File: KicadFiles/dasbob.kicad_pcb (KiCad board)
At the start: 2 copper layers, 243.5 x 104.8 mm, 64 parts, among them J1 TRRS LEFT, J2 TRRS LEFT, SW1 SW_Push, SW10 SW_Push, SW11 SW_Push, SW12 SW_Push, SW13 SW_Push, SW14 SW_Push, SW15 SW_Push, SW16 SW_Push, SW17 SW_Push, SW18 SW_Push, SW19 SW_Push, SW2 SW_Push, SW20 SW_Push, SW21 SW_Push, SW22 SW_Push, SW23 SW_Push, SW24 SW_Push, SW25 SW_Push, SW26 SW_Push, SW27 SW_Push, SW28 SW_Push, SW29 SW_Push, SW3 SW_Push, SW30 SW_Push, SW31 SW_Push, SW32 SW_Push, SW33 SW_Push, SW34 SW_Push, SW35 SW_Push, SW36 SW_Push, SW4 SW_Push, SW5 SW_Push, SW6 SW_Push, SW7 SW_Push, SW8 SW_Push, SW9 SW_Push, U1 Elite-C RIGHT, U2 Elite-C LEFT, U3 OLED1, U4 OLED2

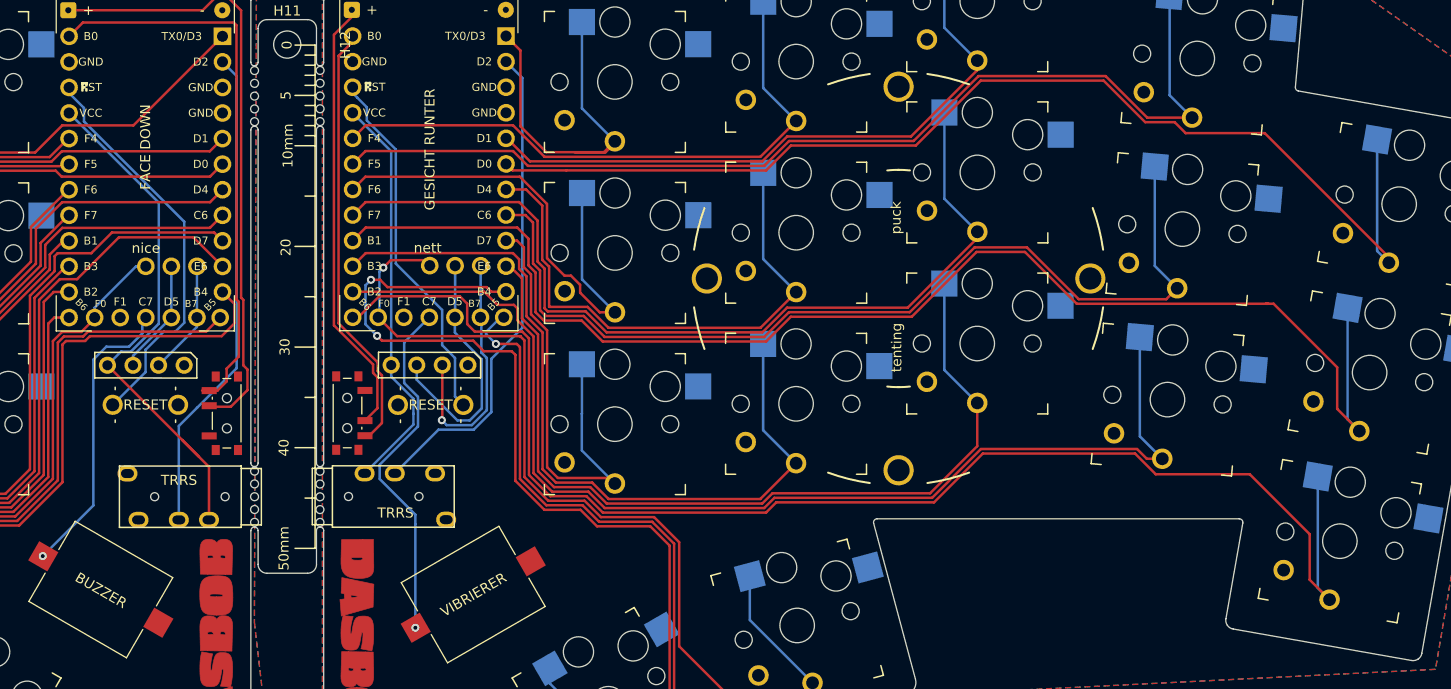
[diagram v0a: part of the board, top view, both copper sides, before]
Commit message: routed the oled to the wrong pins because im a ducking idiot now i fixed it
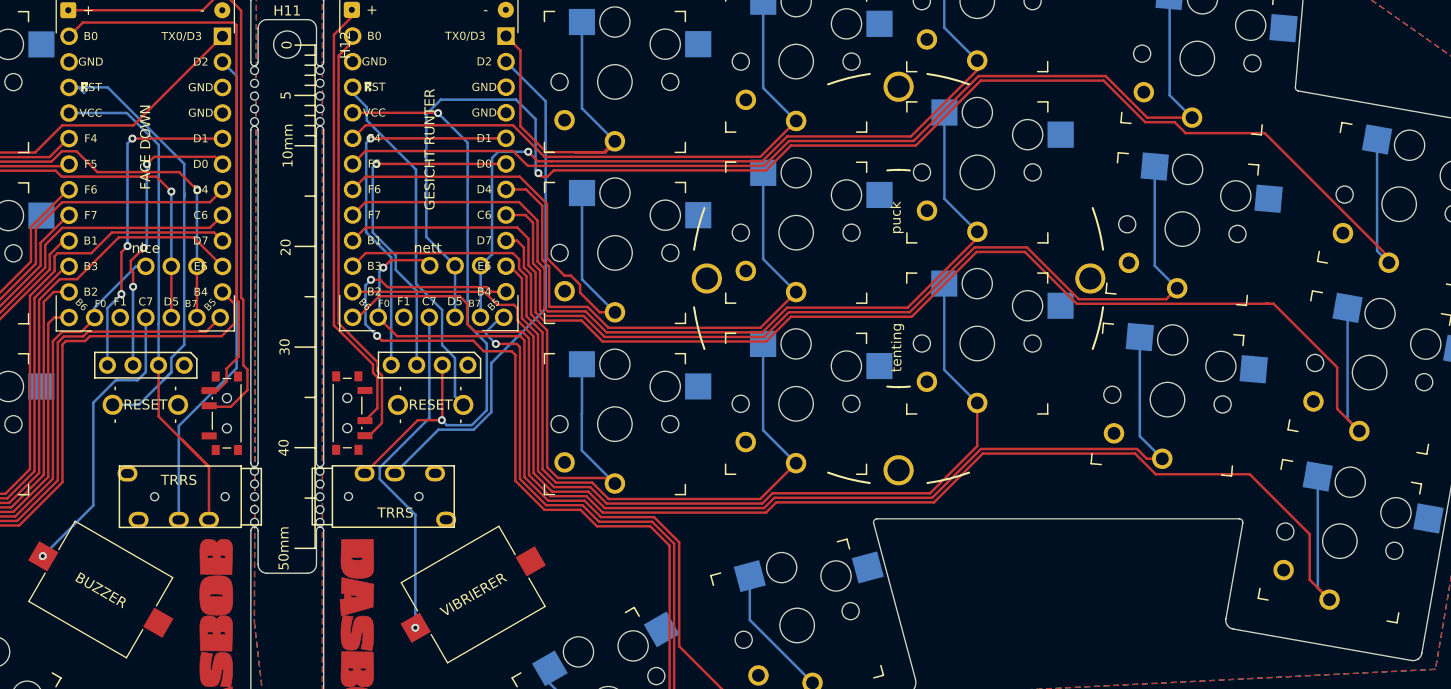
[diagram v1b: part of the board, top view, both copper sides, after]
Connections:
- H5 pad 1: P1 -> 3
- H6 pad 1: P2 -> 1
- H7 pad 1: 1P -> 3a
- H8 pad 1: 2P -> 1a
- U1 pad 25: P1 -> 3
- U1 pad 26: P2 -> 1
- U1 pad 5: 3 -> P1
- U1 pad 6: 1 -> P2
- U2 pad 25: 1P -> 3a
- U2 pad 26: 2P -> 1a
- U2 pad 5: 3a -> 1P
- U2 pad 6: 1a -> 2P
- U3 pad 2: P1 -> VCC
- U3 pad 4: VCC -> P1
- U4 pad 2: 1P -> CVV
- U4 pad 4: CVV -> 1P
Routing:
- net 1a: track 111.7 -> 147.7 mm, vias 0 -> 1
- net P1: track 11.4 -> 32.6 mm, vias 0 -> 3
- net CVV: track 40.3 -> 60.8 mm, vias 0 -> 2
- net 3a: track 65.7 -> 83.2 mm, vias 0 -> 1
- net P2: track 11.4 -> 28.9 mm, vias 0 -> 3
- net 1P: track 25.4 -> 37.3 mm
- net 3: track 80.5 -> 91.7 mm, vias 0 -> 1
- net 2P: track 25.4 -> 35.1 mm, vias 0 -> 1
- net 1: track 128.3 -> 135.9 mm, vias 0 -> 1
- net RST: track 39.2 -> 46.1 mm
- net VCC: track 53.3 -> 55.7 mm
- net 1R: track 48.9 -> 50.8 mm
- net DNUOS: track 35.5 -> 34.4 mm

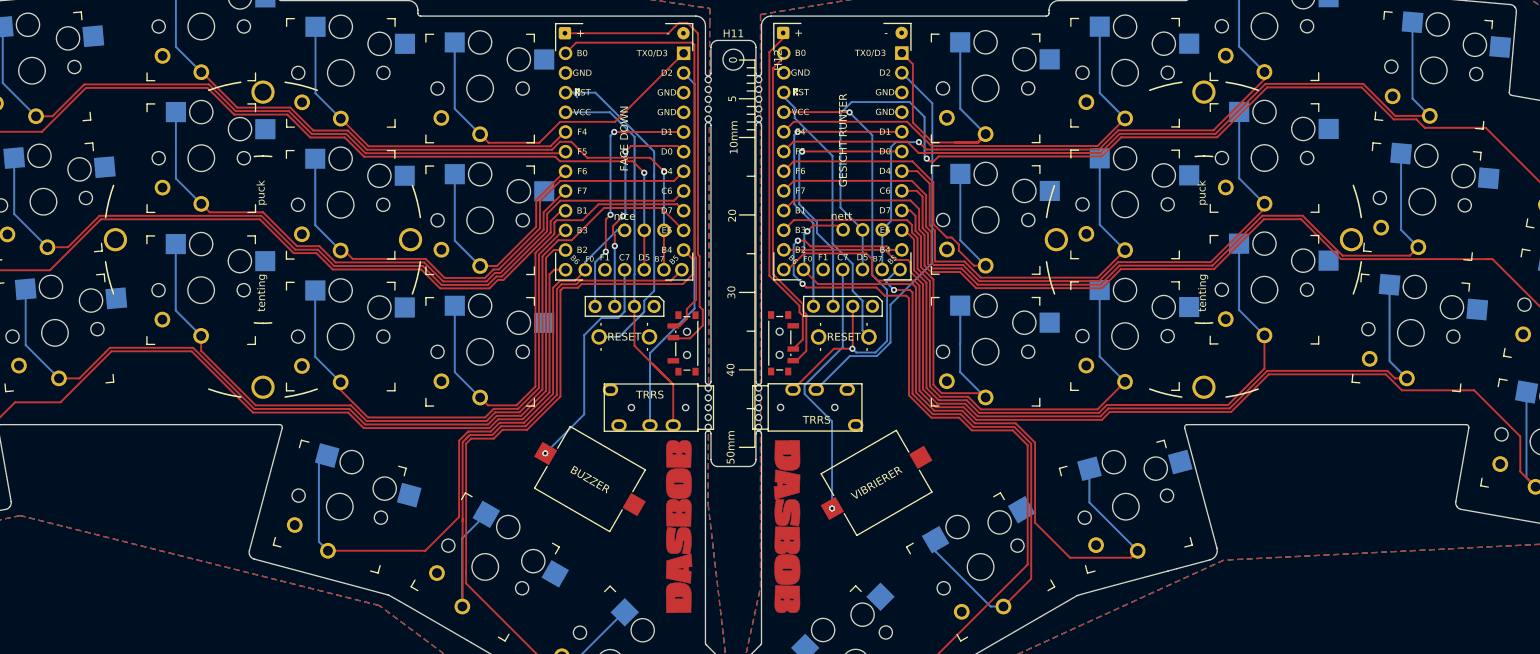
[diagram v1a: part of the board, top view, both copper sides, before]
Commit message: buzzer was not working
buzzer was not working put a jumper for it on the board
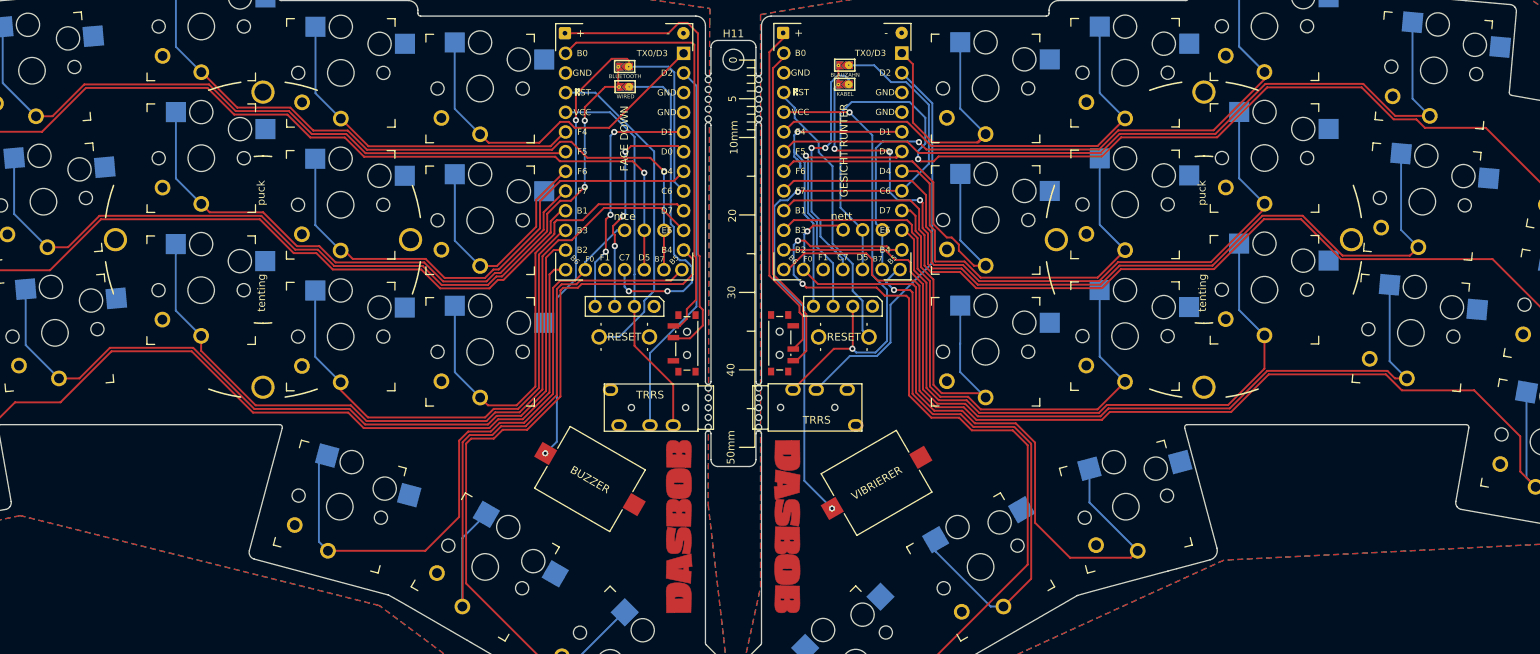
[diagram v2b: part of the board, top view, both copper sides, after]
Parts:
- added JP1: BLUETOOTH, keebio:JUMPER_SMD_2DUB, F.Cu at (139.0, 41.2)
- added JP2: WIRED, keebio:JUMPER_SMD_2DUB, F.Cu at (139.0, 43.9)
- added JP3: BLAUZAHN, keebio:JUMPER_SMD_2DUB, F.Cu at (167.4, 41.1)
- added JP4: KABEL, keebio:JUMPER_SMD_2DUB, F.Cu at (167.4, 43.5)
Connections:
- U1 pad 27: SOUND -> C7
- U1 pad 8: 7 -> SOUND
- U2 pad 27: DNUOS -> C7a
- U2 pad 8: 7a -> DNUOS
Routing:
- net SOUND: track 29.3 -> 79.6 mm, vias 1 -> 2
- net DNUOS: track 34.4 -> 84.4 mm, vias 1 -> 2
- net C7: track 0.00 -> 43.2 mm, vias 0 -> 2
- net C7a: track 0.00 -> 33.2 mm, vias 0 -> 2
- net 7a: track 95.7 -> 120.3 mm, vias 0 -> 3
- net VCC: track 55.7 -> 49.6 mm
- net 7: track 107.1 -> 113.0 mm, vias 0 -> 2
- net 1P: track 37.3 -> 40.6 mm
- net RST: track 46.1 -> 43.0 mm
- net 5a: track 38.0 -> 35.0 mm
- net 3a: track 83.2 -> 84.9 mm
- net 17a: track 74.6 -> 73.0 mm
- net 1a: track 147.7 -> 149.2 mm
- net 17: track 81.0 -> 80.0 mm
- net PWR: track 56.1 -> 55.4 mm
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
